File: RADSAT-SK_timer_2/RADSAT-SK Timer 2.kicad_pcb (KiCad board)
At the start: 2 copper layers, 90.2 x 95.9 mm, 69 parts, among them J201 Conn_01x07, J202 Conn_01x05_Female, J203 Conn_01x03, J204 Conn_01x02, J205 Conn_01x02, J206 Conn_01x02, J207 Conn_02x26_Odd_Even, J208 Conn_02x26_Odd_Even, Q204 IRLML2060, Q205 IRLML2060, Q206 IRLML2060, SW201 SW_Push, SW202 SW_Push, SW203 SW_Push, SW204 SW_Push, SW205 SW_Push, SW206 SW_Push, U101 LT1521IS8-5TR, U202 TPS3700DDCR, U230 CPC1114N, U240 CPC1114N, U250 CPC1114N, U260 CPC1114N

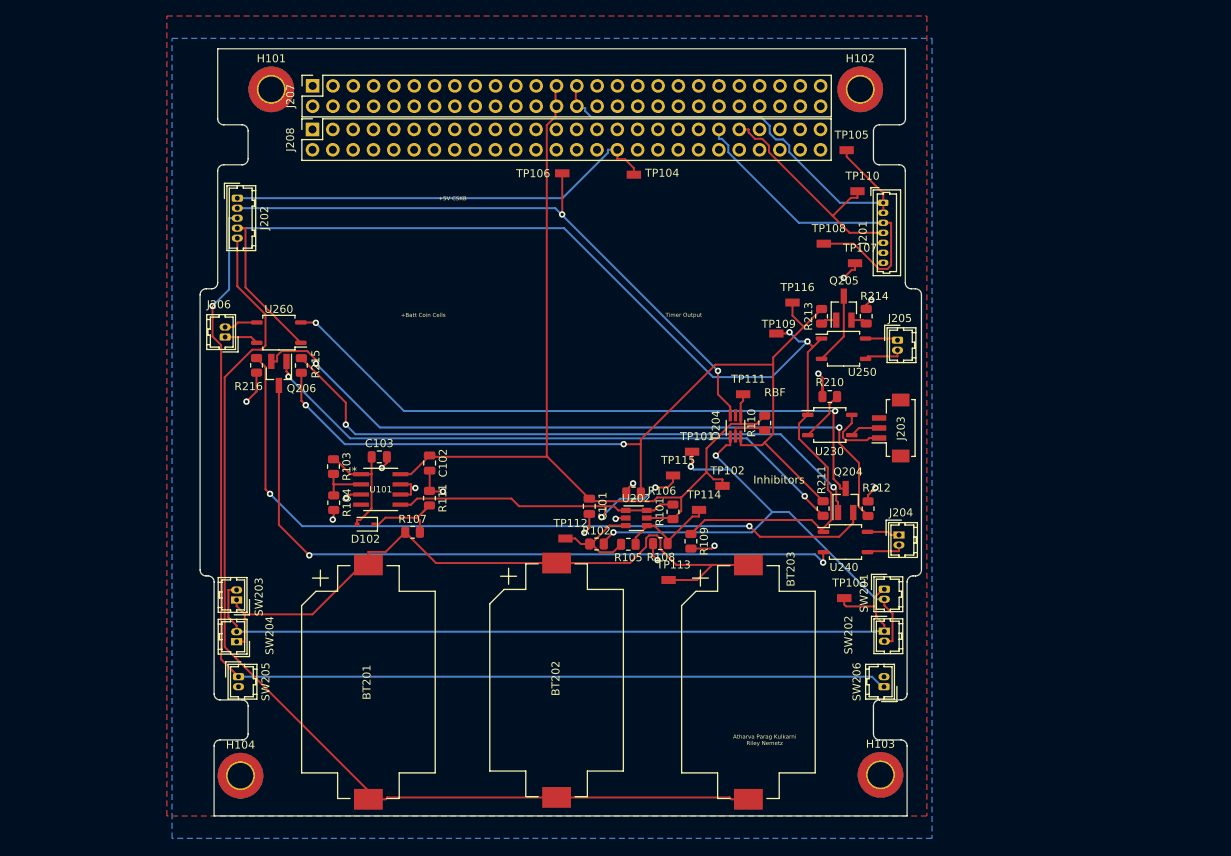
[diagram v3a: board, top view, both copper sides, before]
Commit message: added galaxia timer in schematic, made footprint for galaxia timer and added to PCB new
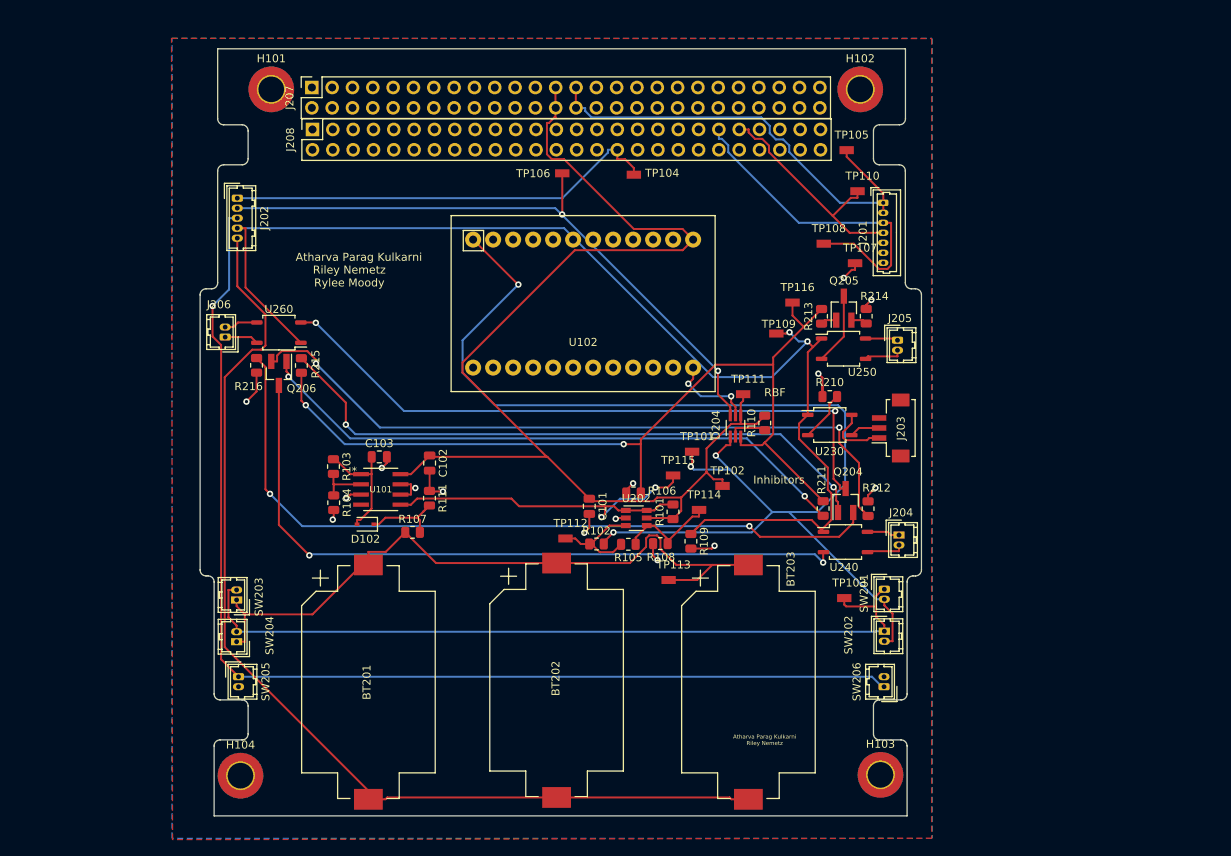
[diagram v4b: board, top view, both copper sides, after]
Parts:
- added U102: Galaxia_Timer, Galaxia_Timer:Galaxia_Timer, F.Cu at (82.7, 81.8)
- U101: value LT1521IS8-5TR -> LT1521
- moved J207 0.22 mm to (48.8, 54.8)
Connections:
- D204 pad 5: (no net) -> Inhib_EN
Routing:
- net B: track 68.4 -> 157.8 mm, vias 3 -> 4
- net +5V: track 115.6 -> 152.1 mm
- net Inhib_EN: track 0.00 -> 10.9 mm, vias 0 -> 2
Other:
- board text added: "Atharva Kulkarni"
- board text added: "Atharva Parag Kulkarni"
- board text added: "Riley Nemetz Rylee Moody"
- board text removed: "+5V CSKB"
- board text removed: "+Batt Coin Cells"
- board text removed: "Timer Output"

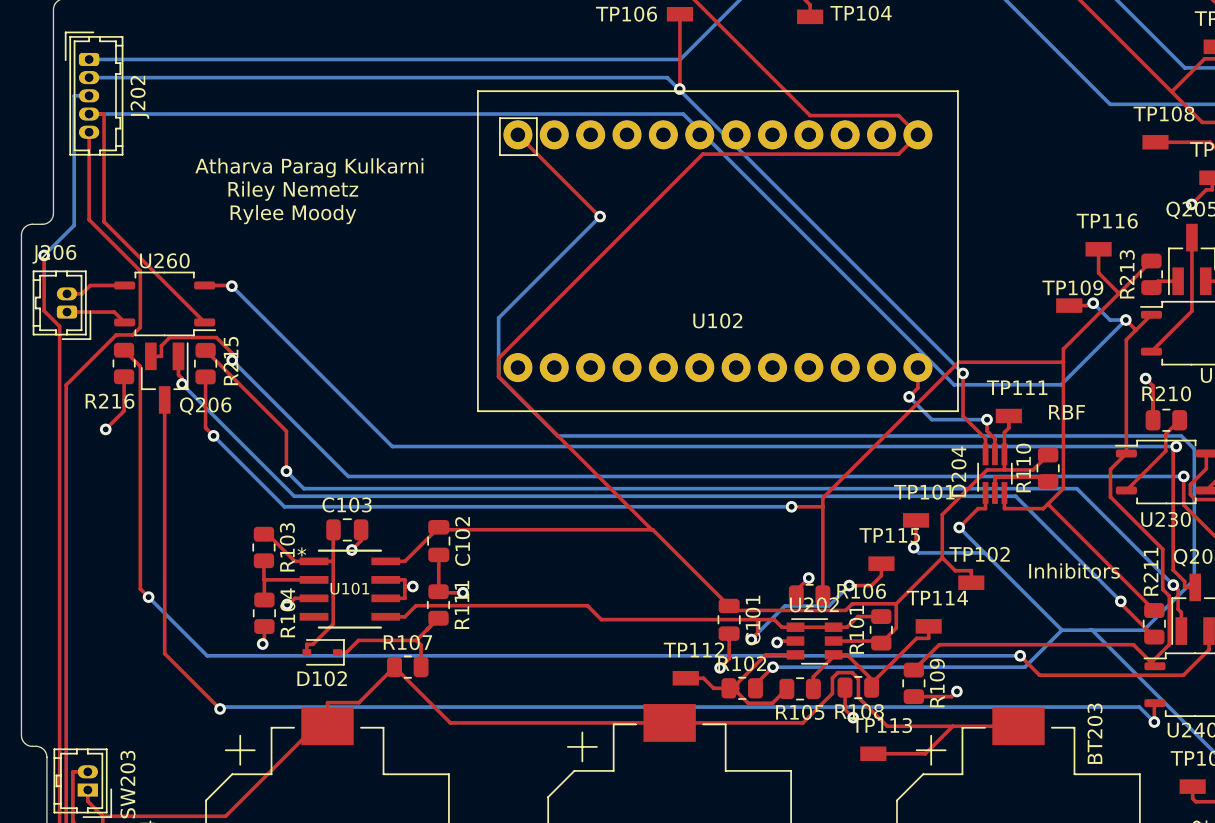
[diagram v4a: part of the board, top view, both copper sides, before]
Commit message: fixed traces
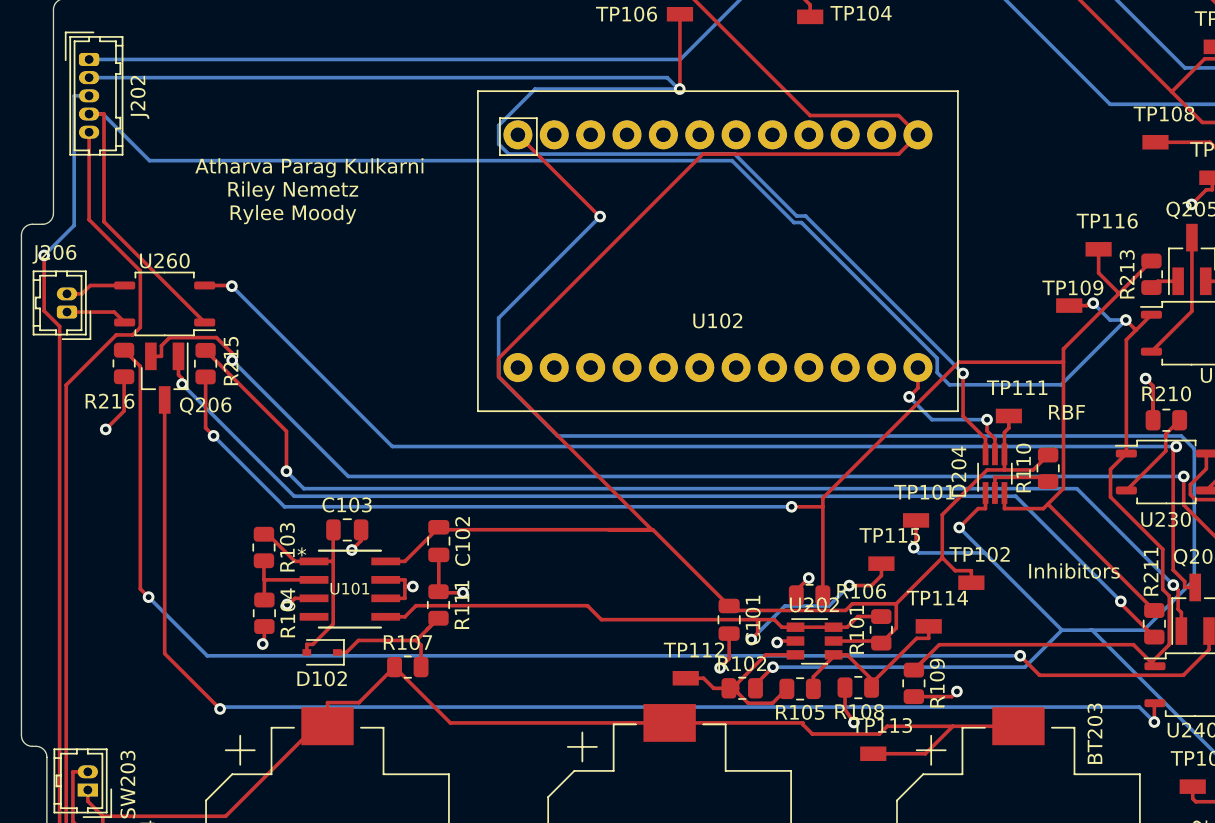
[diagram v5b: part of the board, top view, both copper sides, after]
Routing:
- net Net-(D204-Pad6): track 79.9 -> 105.6 mm
- net A: track 87.3 -> 83.6 mm
- net +5V: track 152.1 -> 155.1 mm
- net InhibV+: track 150.9 -> 151.5 mm
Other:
- board text added: "Luc Charbonneau Lucus Rowlands"

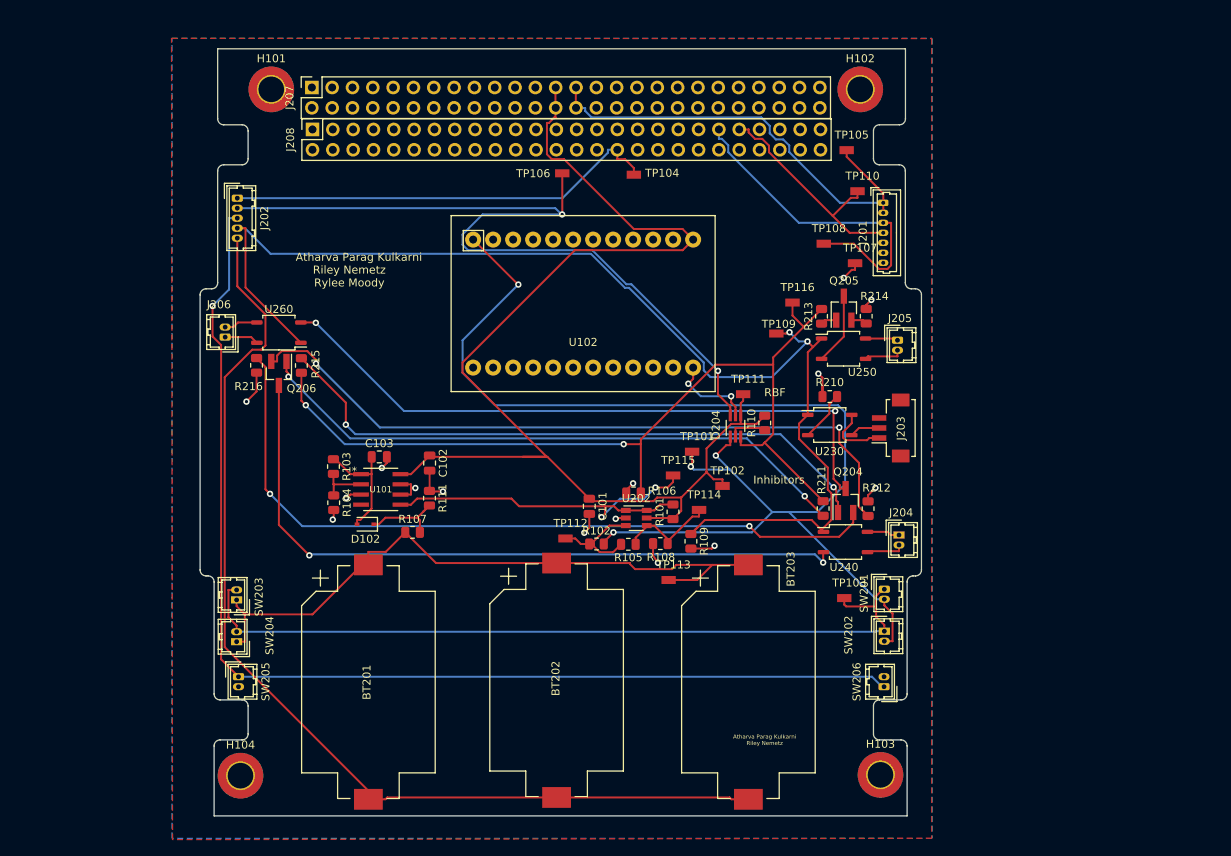
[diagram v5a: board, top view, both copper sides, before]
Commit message: swapped antenna connector and RBF port, pushed switches closer to the coin cells and moved silk screen out of vias
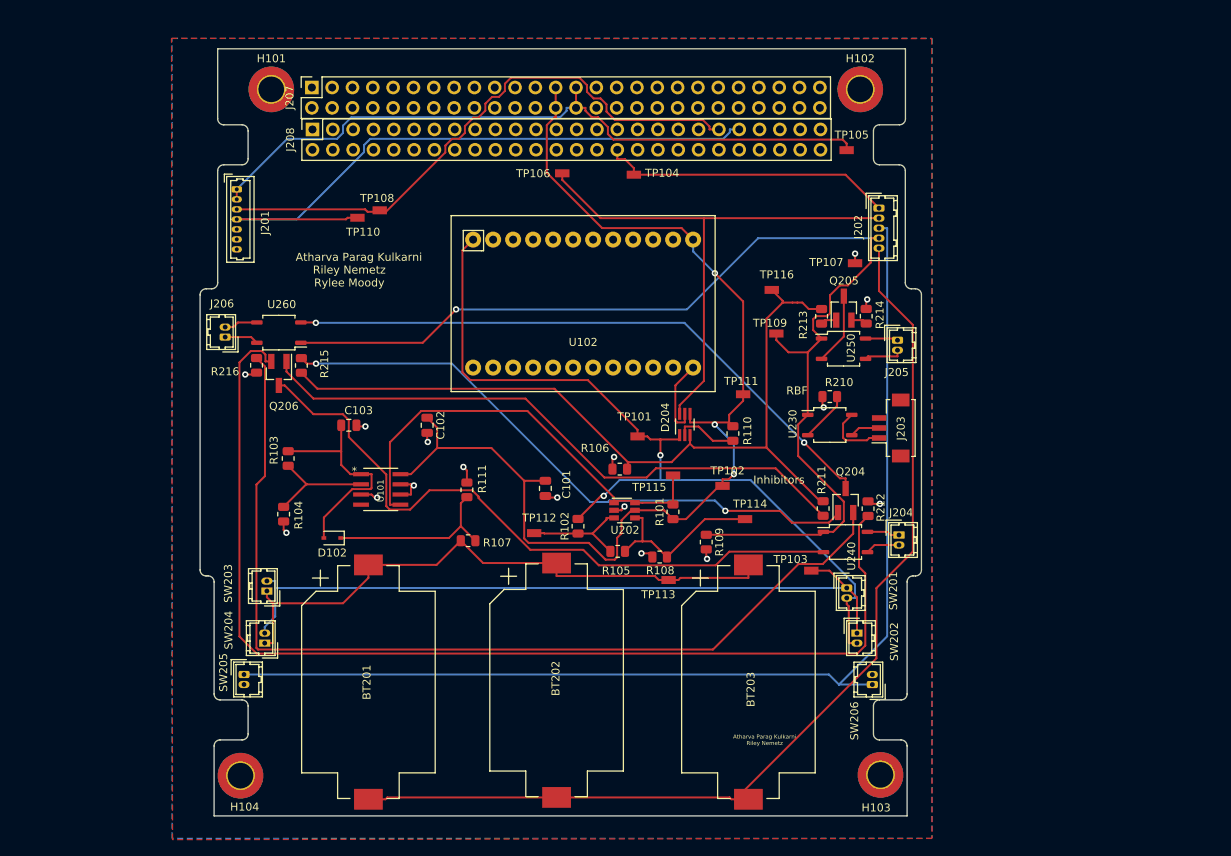
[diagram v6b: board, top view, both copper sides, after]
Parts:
- moved J201 80.8 mm to (39.4, 67.6)
- moved J202 80.2 mm to (119.7, 69.9)
- moved TP110 62.6 mm to (54.5, 71.1)
- moved TP108 55.7 mm to (57.3, 70.2)
- moved TP101 7.08 mm to (89.5, 98.5)
- moved R107 7.02 mm to (68.3, 111.5)
- moved R104 6.42 mm to (45.3, 108.2)
- moved D204 6.34 mm to (95.4, 97.0)
- moved C101 5.93 mm to (78.0, 105.0)
- moved TP114 5.86 mm to (103.0, 108.8)
- moved R103 5.75 mm to (45.8, 101.2)
- moved C103 5.49 mm to (53.4, 97.1)
- moved TP103 5.36 mm to (111.2, 115.2)
- moved R111 4.79 mm to (68.2, 105.1)
- moved C102 4.73 mm to (63.2, 97.1)
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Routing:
- net I2C_CLK: track 28.9 -> 83.4 mm
- net B: track 157.8 -> 105.4 mm, vias 4 -> 2
- net Net-(Q206-Pad2): track 89.5 -> 136.4 mm, vias 2 -> 0
- net Net-(D204-Pad6): track 105.6 -> 68.1 mm, vias 2 -> 0
- net +3V3: track 57.5 -> 88.4 mm
- net I2C_DATA: track 42.8 -> 73.3 mm
- net Net-(Q204-Pad2): track 94.8 -> 120.4 mm, vias 2 -> 0
- net USB_Charge: track 54.8 -> 36.9 mm
- net +5V: track 155.1 -> 141.6 mm, vias 0 -> 3
- net Net-(C103-Pad1): track 15.0 -> 27.6 mm
- net GND: track 39.3 -> 27.0 mm, vias 15 -> 16
- net Net-(D102-Pad1): track 11.0 -> 22.1 mm
- net /Inhib_in: track 113.1 -> 102.1 mm, vias 2 -> 0
- net Net-(R105-Pad1): track 12.9 -> 22.2 mm
- net Net-(R103-Pad2): track 6.12 -> 14.1 mm
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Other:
- board text added: "June 22, 2022"
- board text removed: "November 6th, 2021"
